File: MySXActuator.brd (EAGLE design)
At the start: 26.4 x 35.6 mm, 9 parts, among them Q1 2N7002, Q2 IRF530, X2 MKDSN1,5/5-5,08

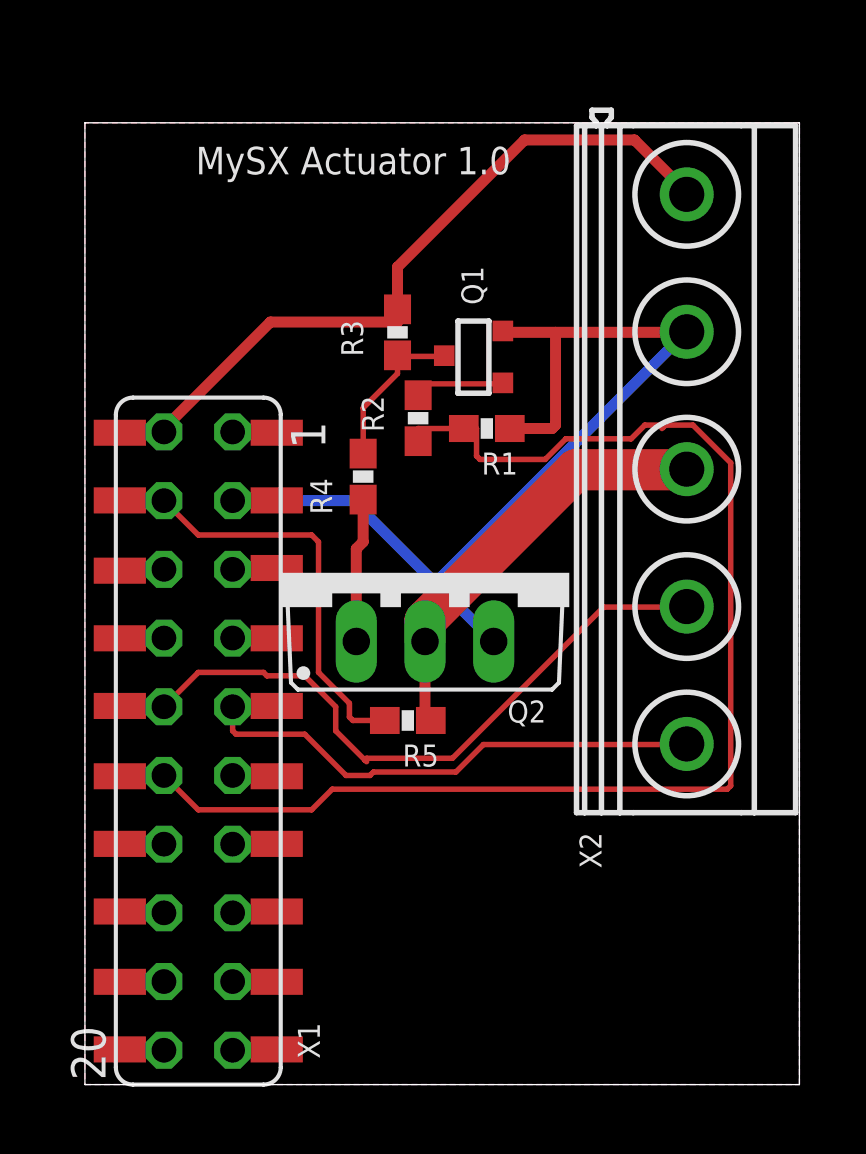
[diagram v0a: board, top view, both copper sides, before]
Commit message: enlarge traces widths + add ldo
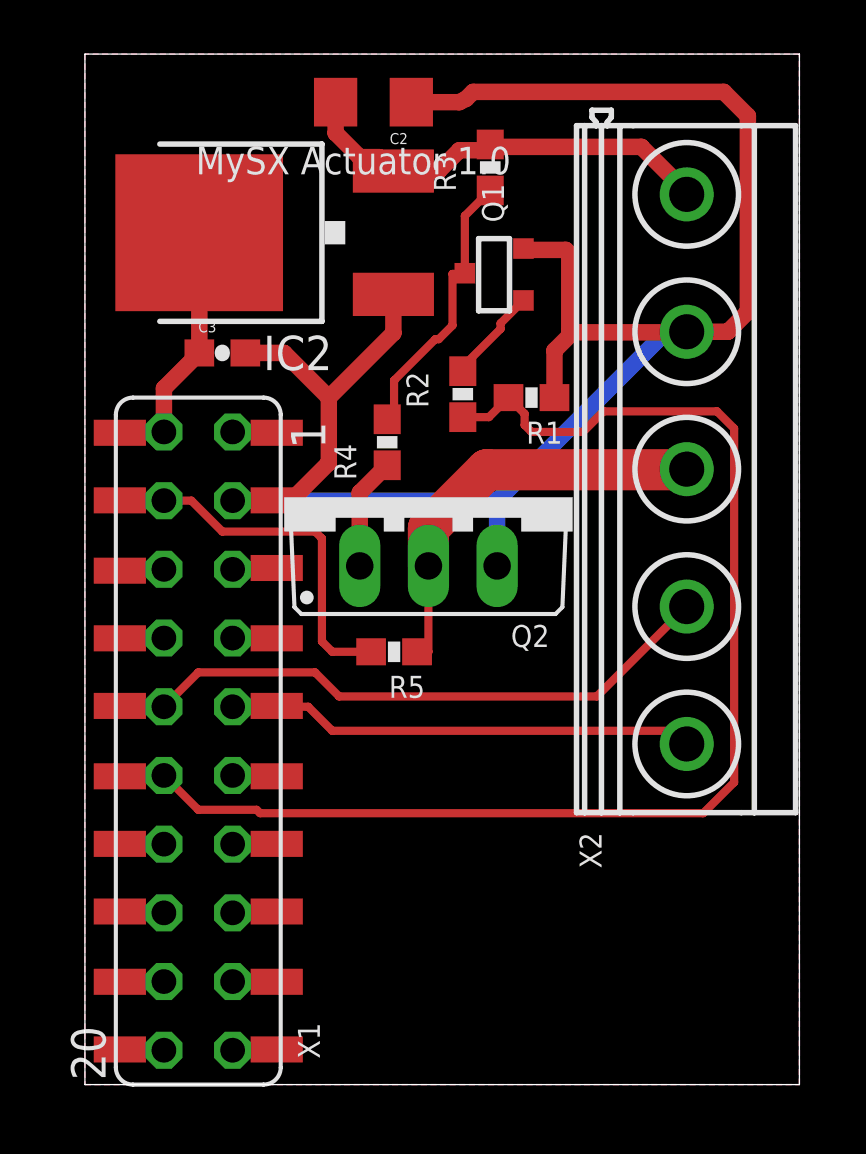
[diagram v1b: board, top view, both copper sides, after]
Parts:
- added C2: 10u, SparkFun-Passives:1206
- added C3: 10u, SparkFun-Passives:0603-CAP
- added IC2: LD117ADT-TR, v-reg:DPACK
- moved R3 6.99 mm to (14.0, 33.9)
- moved Q1 3.14 mm to (14.1, 30.0)
- moved Q2 2.80 mm to (11.7, 21.7)
- moved R5 2.59 mm to (10.4, 16.0)
- moved R1 2.01 mm to (15.5, 25.4)
- moved R2 1.88 mm to (13.0, 25.5)
- moved R4 1.55 mm to (10.2, 23.7)
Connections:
- new net 12V: C2.2, IC2.3, R3.2, X2.1
- net GND: now also C2.1, C3.2, IC2.1
- net VRAW: now also C3.1, IC2.4; no longer R3.2, X2.1
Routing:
- net GND: track 37.0 -> 71.4 mm
- net VRAW: track 25.9 -> 7.91 mm
- net 12V: track 0.00 -> 16.0 mm
- net N$12: track 5.89 -> 10.4 mm
- net D3_INT: track 24.2 -> 21.6 mm
- net VCCIO: track 14.7 -> 12.2 mm
- net D4_INT: track 18.8 -> 17.4 mm
- net D5_PWM: track 48.1 -> 46.9 mm
- net N$13: track 5.35 -> 4.14 mm
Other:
- board size 26.4 x 35.6 mm -> 26.4 x 38.1 mm

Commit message: add second dimmer
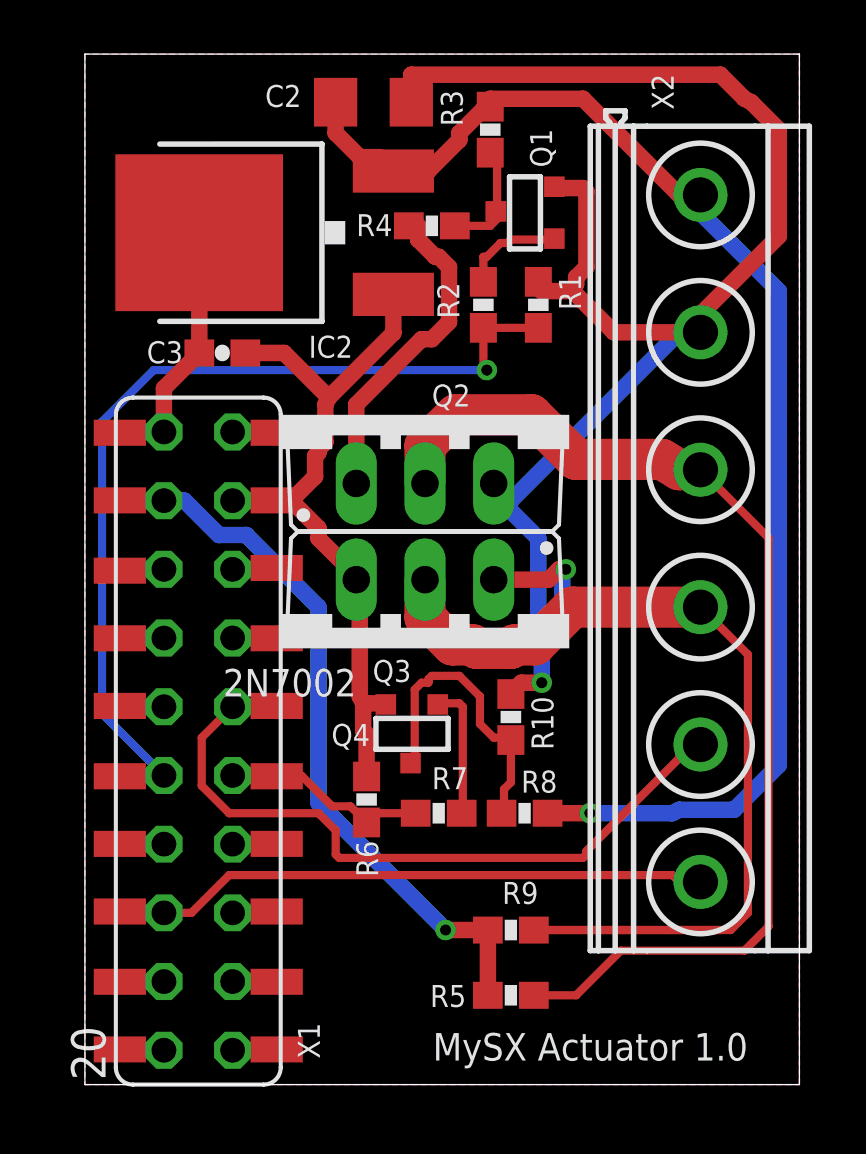
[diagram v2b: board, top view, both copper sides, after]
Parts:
- added Q3: IRF530, transistor-power:TO220BV
- added Q4: 2N7002, transistors:SOT-23
- added R10, R7: 27, SparkFun-Passives:0603-RES
- added R6, R8, R9: 10k, SparkFun-Passives:0603-RES
- X2: value MKDSN1,5/5-5,08 -> MKDSN1,5/6-5,08; device con-phoenix-508:MKDSN1,5/5-5,08 -> con-phoenix-508:MKDSN1,5/6-5,08
- moved R5 13.4 mm to (14.7, 3.30)
- moved R4 8.17 mm to (11.8, 31.8), turned to 0 degrees
- moved R1 3.44 mm to (15.7, 28.8), turned to 270 degrees
- moved R2 3.39 mm to (13.7, 28.8)
- moved Q2 3.05 mm to (11.6, 24.8)
- moved X2 2.59 mm to (21.7, 20.2)
- moved Q1 2.56 mm to (15.2, 32.3)
- moved R3 1.40 mm to (14.0, 35.3)
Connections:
- net N$10 renamed LED1
- new net LED2: Q3.D, R9.1, X2.4
- new net N$2: Q4.1, R7.2
- new net N$3: Q4.3, R10.2, R8.1
- new net N$4: Q3.G, R10.1
- net 12V: now also R8.2
- net D3_INT: no longer X2.4
- net D6_PWM: now also R6.2, R7.1
- net D9_A3: now also X2.6
- net GND: now also Q3.S, Q4.2, R6.1
- net VCCIO: now also R9.2
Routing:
- net LED2: track 0.00 -> 39.8 mm
- net 12V: track 16.0 -> 49.6 mm, vias 0 -> 1
- net LED1: track 15.4 -> 40.5 mm
- net D3_INT: track 21.6 -> 0.00 mm
- net D9_A3: track 0.00 -> 20.5 mm
- net GND: track 71.4 -> 86.5 mm, vias 0 -> 1
- net D5_PWM: track 46.9 -> 32.7 mm, vias 0 -> 1
- net VCCIO: track 12.2 -> 25.2 mm, vias 0 -> 1
- net N$3: track 0.00 -> 11.3 mm
- net N$4: track 0.00 -> 8.80 mm, vias 0 -> 2
- net D4_INT: track 17.4 -> 25.6 mm
- net N$13: track 4.14 -> 12.1 mm
- net D6_PWM: track 0.00 -> 7.68 mm
- net N$12: track 10.4 -> 4.44 mm
- net N$2: track 0.00 -> 4.97 mm
